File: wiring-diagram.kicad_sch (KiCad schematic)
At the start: 5 parts

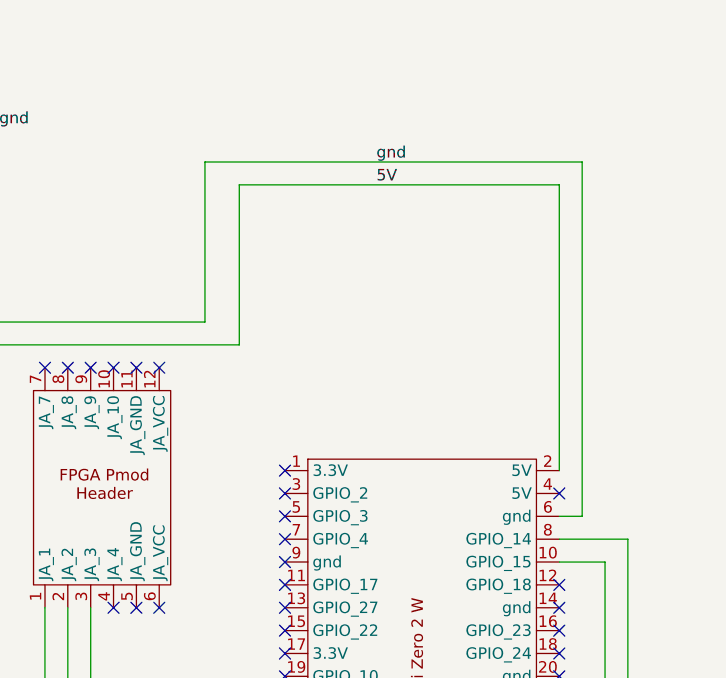
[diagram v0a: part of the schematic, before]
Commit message: switch 5V wire to rpi
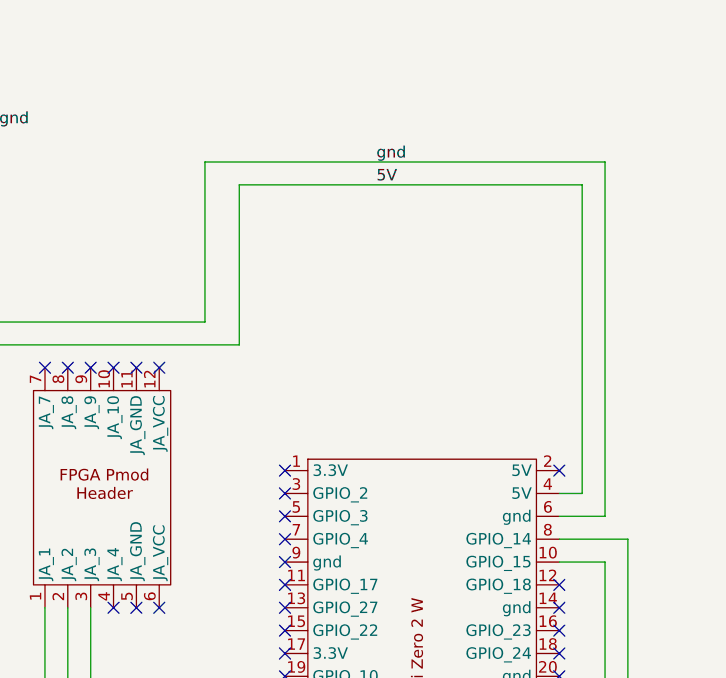
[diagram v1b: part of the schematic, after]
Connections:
- net 5V: now also U4.4 (5V); no longer U4.2 (5V)
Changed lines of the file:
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@@
+	)
+	(no_connect
+		(at 212.09 97.79)
 	)
 	(no_connect
@@
 	)
 	(no_connect
-		(at 212.09 100.33)
-	)
-	(no_connect
 		(at 143.51 92.71)
 	)
@@
 	(wire
 		(pts
+			(xy 214.63 66.04) (xy 214.63 100.33)
+		)
+		(stroke
+			(width 0)
+			(type default)
+		)
+	)
+	(wire
+		(pts
 			(xy 217.17 107.95) (xy 212.09 107.95)
 		)
@@
 	(wire
 		(pts
-			(xy 214.63 63.5) (xy 214.63 102.87)
+			(xy 217.17 63.5) (xy 217.17 102.87)
 		)
 		(stroke
@@
 	(wire
 		(pts
-			(xy 172.72 63.5) (xy 214.63 63.5)
+			(xy 172.72 63.5) (xy 217.17 63.5)
 		)
 		(stroke
@@
 	(wire
 		(pts
-			(xy 176.53 66.04) (xy 212.09 66.04)
+			(xy 176.53 66.04) (xy 214.63 66.04)
 		)
 		(stroke
@@
 	(wire
 		(pts
-			(xy 214.63 102.87) (xy 212.09 102.87)
+			(xy 217.17 102.87) (xy 212.09 102.87)
 		)
 		(stroke
@@
 	(wire
 		(pts
-			(xy 212.09 66.04) (xy 212.09 97.79)
-		)
-		(stroke
+			(xy 214.63 100.33) (xy 212.09 100.33)
+		)
+		(stroke
